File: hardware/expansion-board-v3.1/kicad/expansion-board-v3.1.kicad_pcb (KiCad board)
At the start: 6 copper layers, 100 x 62 mm, 156 parts, among them J1 PinHeader_2x20_P2.54mm_Vertic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, J2 U.FL_Hirose_U.FL-R-SMT-1_Vert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, J4 USB_C_Receptacle_HRO_TYPE-C-3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, J5 U.FL_Hirose_U.FL-R-SMT-1_Vert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, J6 U.FL_Hirose_U.FL-R-SMT-1_Vert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, J8 U.FL_Hirose_U.FL-R-SMT-1_Vert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, Q2 SOT-23, Q3 SOT-23, Q4 SOT-23, Q5 SOT-23, SW1 SolderJumper-2_P1.3mm_Open_Pa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, SW2 SolderJumper-2_P1.3mm_Open_Pa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, U1 SOT-23-5, U10 QFN-48-1EP_7x7mm_P0.5mm_EP5.1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, U11 DFN-8-1EP_2x2mm_P0.5mm_EP0.86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, U12 SOT-363_SC-70-6, U13 AD8319_LFCSP-8-EP, U14 MSOP-8_3x3mm_P0.65mm, U15 SOT-23-6, U16 SOT-363_SC-70-6, U17 SOT-363_SC-70-6, U2 SOT-23-5, U3 SOT-23-5, U4 BNO085_LGA-28, U5 BMP388_LGA-10, U6 LGA-16_3x3mm_P0.5mm, U7 ATGM336H_LCC-18, U8 QFN-56-1EP_7x7mm_P0.4mm_EP3.2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, U9 SOIC-8_5.3x5.3mm_P1.27mm, Y1 Crystal_SMD_3225-4Pin_3.2x2.5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, Y2 Crystal_SMD_3225-4Pin_3.2x2.5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, Y3 Crystal_SMD_3215-2Pin_3.2x1.5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

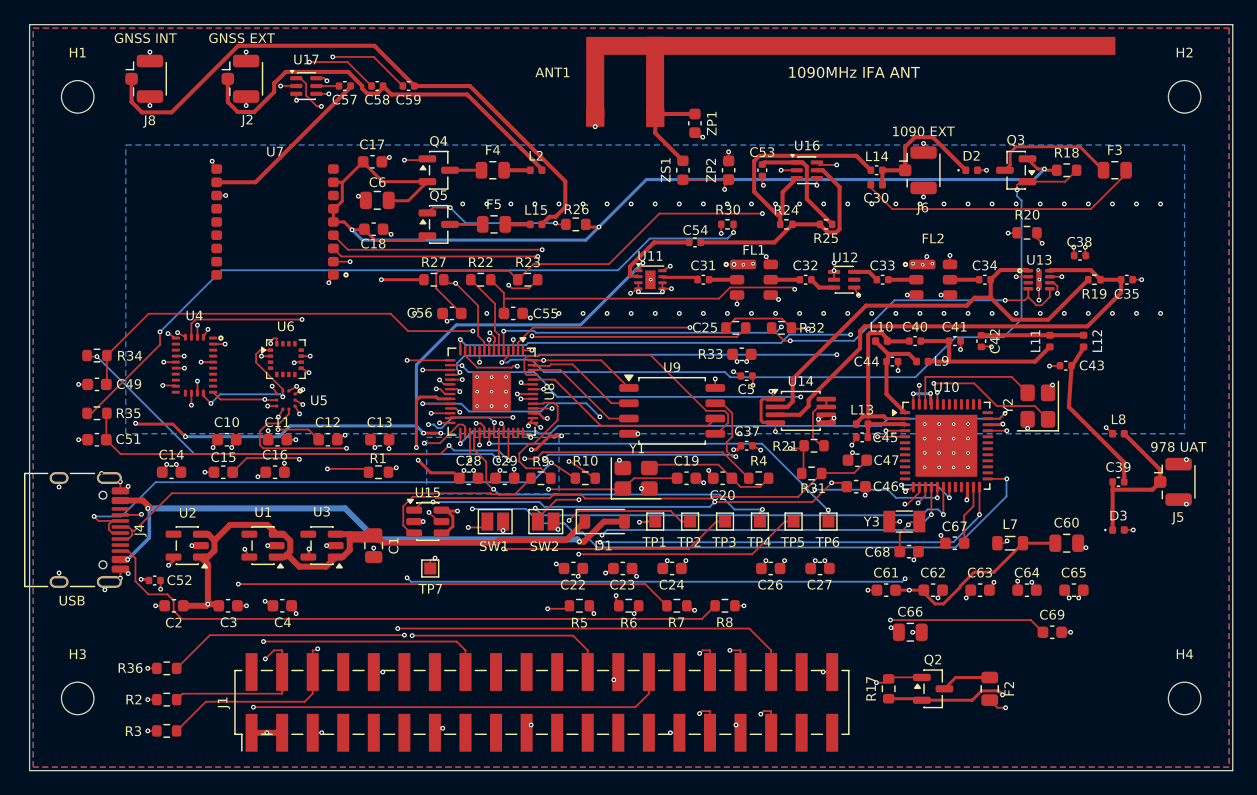
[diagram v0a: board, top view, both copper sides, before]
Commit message: feat(hw): 重排布局布线 + IC 型号标注 —— 全绿，Gerber 已出
评审挪了元件、重拉了线、删掉重排了自动生成的走线、加了 GND 缝合孔，
要求检查 + 在 IC 中心标型号 + 固化 + 出 Gerber。

    未连通 0 / 铜层 DRC 0 违例 / 丝印 overlap 1 / over_copper 1 / edge 2
    走线 1428 段 / 过孔 469 个   射频 165 段全 F.Cu、0 过孔
    rebuild 逐坐标 100% 复现（走线/过孔/板级文字/位号/元件坐标全部 0 不一致）

## 检查出 7 项并全部修掉

  · holes_co_located ×3 —— 加 GND 孔时在 (97.012,57.727) 同一点叠了 3 个（重复点击）
  · track_dangling SUBG_FEED —— 0.27mm 残线，另一端已是三线交汇点，删掉不影响连通
  · track_dangling SUBG_N5 —— 两段在 82.275~82.860 重叠成 **T 接**。电气上是通的
    （未连通=0 证明），但 KiCad 要求端点对端点，端点落在另一条线**中间**判 dangling。
    把起点提到 82.860 与之首尾相接
  · clearance ×2 —— 新加的两个 GND 缝合孔离 SUBG_MISO 只有 0.1255mm（要 0.15）。
    缝合孔哪儿都能打，沿法向挪 0.10mm

删除时踩了个老坑：`board.Remove()` 之后在**同一进程**里跑 ZONE_FILLER，
被删的线又回来了（route_fix.py:26 记过 SWIG 状态不可靠）。拆成三个独立进程：
改坐标 → 删除 → 重灌，才真正生效。

## IC 型号标注：17 条，但只有 1 条能真印

新增 gen_u_labels.py。判据迭代了三轮，每轮都是被 DRC 打回来的：

  ① 只查中心点是否落在焊盘上 → 报 29 条 silk_over_copper
     文字**有宽度**，BNO085 那串宽 4.5mm 横跨整颗芯片、压住左右两排引脚
  ② 改用文字包围盒，但只试横排 → 17 颗里只有 2 颗能印
     **横排压焊盘不代表竖排也压**：SOT-23-5 这类两侧排焊盘的封装，
     中间那条竖缝往往容得下竖排
  ③ 横竖都试之后仍报 17 条 over_copper，两个原因：
     · **CHAR_W 取 0.62 严重低估** —— KiCad 描边字体字宽≈字高、加字距约 1.1×h。
       系数错了，后面所有几何判断都白算
     · hits() 只查元件**自己**的焊盘 —— 实测 U14 的 'AD8313' 压到了隔壁 R21

用正确的字宽算下来：**只有 U7(ATGM336H) 一颗印得上**。这是物理现实——
IC 中心两侧就是引脚焊盘，型号串放进去必然压焊盘。其余 16 条进 F.Fab：
不参与印刷、不影响制造，但 KiCad 里看得见、assembly-top.pdf 里有。
最终丝印违例**没有增加**（还是原有的 1/1/2），证明 17 条全部落在合法位置。

三路 LDO 的标注用**功能标识**而非型号（3V3-D / 3V3-RF / 3V3-G）：
TPS7A2033 放进 SOT-23-5 只有 0.70mm 字高、低于可印下限，而且对着空板调试时
想知道的本来就是"这颗出什么电"，料号在 BOM 和装配图里有。

## Gerber

fab/expansion-board-v3.1-fab.zip（18 个文件）+ positions.csv
硬门槛通过：未连通 0、铜层违例 0。
下单四项确认见 tools/gerber.sh 输出（6 层叠层顺序 / POFV 树脂塞孔 /
最小孔径线宽 0.15 / 板厚 1.6mm 无铅）。
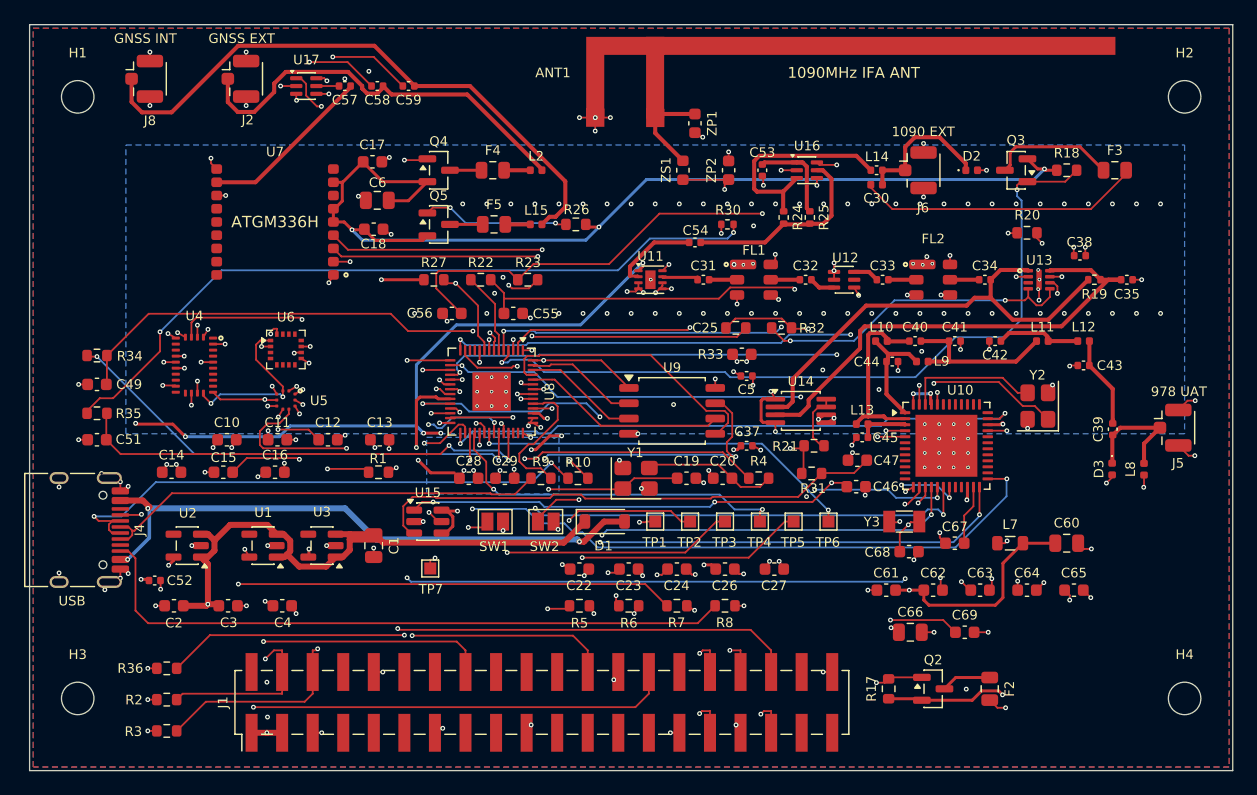
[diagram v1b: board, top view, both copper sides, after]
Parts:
- moved C69 7.28 mm to (127.7, 100.5)
- moved D3 5.09 mm to (140.0, 86.9), turned to -90 degrees
- moved J5 4.50 mm to (145.5, 83.5)
- moved C39 4.40 mm to (140.0, 83.6), turned to -90 degrees
- moved C26 3.80 mm to (107.8, 95.2)
- moved C27 3.80 mm to (111.9, 95.2)
- moved L8 3.64 mm to (142.6, 87.0), turned to 90 degrees
- moved C43 1.48 mm to (137.6, 78.3)
- moved R25 1.47 mm to (114.8, 66.0), turned to -90 degrees
- moved C42 1.15 mm to (130.2, 76.3), turned to 180 degrees
- moved U6 0.80 mm to (71.3, 77.0)
- moved L11 0.62 mm to (134.2, 76.3), turned to 0 degrees
- moved R24 0.62 mm to (112.7, 66.0), turned to -90 degrees
- moved R10 0.61 mm to (95.6, 87.7)
- moved C22 0.50 mm to (95.7, 95.2)
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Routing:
- net GND: track 100.1 -> 108.9 mm, vias 221 -> 237
- net SUBG_X32K2: track 32.7 -> 25.4 mm
- net SUBG_N5: track 13.6 -> 7.65 mm
- net ANT_978: track 13.5 -> 10.0 mm
- net SW1_J1: track 18.5 -> 16.4 mm
- net SUBG_VDDR: track 36.6 -> 38.6 mm
- net SW1_J3: track 9.59 -> 7.73 mm
- net SW1_J2: track 20.3 -> 18.4 mm
- net 3V3_DIG: track 37.9 -> 39.5 mm
- net SUBG_N4: track 8.50 -> 7.13 mm
- net SUBG_FEED: track 29.1 -> 27.7 mm
- net USB_CC2: track 53.8 -> 55.1 mm
- net SUBG_N3: track 14.8 -> 13.8 mm
- net QMC_C1: track 15.2 -> 16.0 mm
- net I2C_SCL: track 52.1 -> 52.9 mm
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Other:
- board text added: "3V3-D"
- board text added: "3V3-G"
- board text added: "3V3-RF"
- board text added: "AD8313"
- board text added: "AD8319"
- board text added: "ATGM336H"
- board text added: "BMP388"
- board text added: "BNO085"
- board text added: "CC1312R"
- board text added: "LNA1"
- board text added: "LNA2"
- board text added: "QMC5883"
- board text added: "RP2040"
- board text added: "SW1090"
- board text added: "SWGNSS"
- board text added: "TLV3501"
- board text added: "W25Q128"

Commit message: fix(hw): 板子版本号 V1 → V1.0，重出 Gerber
产品要求：「板子的版本号是 1.0，改过来，然后重新生成 Gerber」。

改了三处，缺一处版本号就会不一致：
    tools/gen_silk.py       BOARD_REV      离线排版工具
    tools/gen_brand_silk.py BOARD_REV      流程里补品牌丝印用
    tools/SILK.json         'V1   2026-08' → 'V1.0   2026-08'

**SILK.json 才是板子的真正来源**——rebuild 从它复现板级文字，
只改两个脚本的常量而不改它，跑一次 rebuild 版本号又变回 V1。

验证：rebuild 后板上 B.Silkscreen (100.0,80.0) 是 'V1.0   2026-08' ✅
    未连通 0 / 铜层 DRC 0 / 丝印 1+1+2（与改版本号前一致）

Gerber 已重出：fab/expansion-board-v3.1-fab.zip（645KB，18 个文件）
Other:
- board text added: "V1.0 2026-08"
- board text removed: "V1 2026-08"

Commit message: fix(hw): 板子版本号改为 V3.1（上一版写成 1.0 是错的）
板子从工程名到目录名都是 v3.1，丝印上写 V1.0 对不上。

改的还是那三处（缺一处，跑一次 rebuild 就退回去）：
    tools/gen_silk.py       BOARD_REV
    tools/gen_brand_silk.py BOARD_REV
    tools/SILK.json         ← 这个才是板子的来源，rebuild 从它复现板级文字

验证：板上 B.Silkscreen (100.0,80.0) = 'V3.1   2026-08'
    未连通 0 / 铜层 DRC 0 / 丝印 1+1+2（与改动前一致）
Gerber 已重出。
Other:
- board text added: "V3.1 2026-08"
- board text removed: "V1.0 2026-08"

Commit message: fix(hw): 最小孔径 0.15 → 0.20mm，省掉嘉立创 200 元工艺费
评审下单时发现：最小孔径选 0.15mm 要**额外加收 200 元**，5 片打样从 300 涨到 500+。

## 那 34 个 0.15mm 孔本来就不该是 0.15

全是 EP 散热孔（thermal_vias.py 用 0.3mm 盘 / 0.15mm 孔），当初的理由是
"盘小才排得密"。但孔心间距后来已经从 0.8mm 放宽到 1.2mm（业界推荐上限），
**1.2mm 间距下 0.4mm 盘和 0.3mm 盘都排得开**——"排得密"这个理由早就不成立了，
等于白付这笔钱。

改完全板过孔统一成 0.4mm 盘 / 0.2mm 孔（466 个），**最小孔径 0.20mm 属普通档**，
不光这次省 200，将来批量下单也一直省着。

    改 31 个：U10 ×16、U8 ×9、FL2 ×3、FL1 ×2、U11 ×1
    删  3 个：U13

## 为什么 U13 那 3 个是删不是改

U13(AD8319) 的 EP 只有 **0.45mm 宽**，而嘉立创要求 0.2mm 孔至少配 0.4mm 盘
（环宽 0.1mm），两边只剩 0.025mm，放不下。

代价可接受：AD8319 是检波器、功耗几十毫瓦，散热完全不需要；EP 顶层仍连在 F.Cu
的 GND 覆铜上，只是少了直下内层地平面的低阻抗路径，射频地回流绕远一点。
这次是原型 5 片，验证完再决定要不要为这 3 个孔付钱。

## 顺带同步 gerber.sh 的下单提示

那几行是供照着勾选项的，写着"最小孔径 0.15mm"和"必须勾 POFV 树脂塞孔"
就白改了。POFV 也不再需要——盘中孔已经从 0.3mm 盘放大到 0.4mm。

验证：未连通 0 / 铜层 DRC 0 / 丝印 1+1+2，全板最小钻孔 0.20mm。
Gerber 已重出。
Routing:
- net GND: vias 237 -> 234
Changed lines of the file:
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@@
 	(via
 		(at 110.13 69.86)
-		(size 0.3)
-		(drill 0.15)
+		(size 0.4)
+		(drill 0.2)
 		(layers "F.Cu" "B.Cu")
 		(net "GND")
@@
 	(via
 		(at 125.6 86.8)
-		(size 0.3)
-		(drill 0.15)
-		(layers "F.Cu" "B.Cu")
-		(net "GND")
-	)
-	(via
-		(at 133.83 71.985)
-		(size 0.3)
-		(drill 0.15)
+		(size 0.4)
+		(drill 0.2)
 		(layers "F.Cu" "B.Cu")
 		(net "GND")
@@
 	(via
 		(at 126.8 83.2)
-		(size 0.3)
-		(drill 0.15)
+		(size 0.4)
+		(drill 0.2)
 		(layers "F.Cu" "B.Cu")
 		(net "GND")
@@
 	(via
 		(at 89.6 79.3)
-		(size 0.3)
-		(drill 0.15)
+		(size 0.4)
+		(drill 0.2)
 		(layers "F.Cu" "B.Cu")
 		(net "GND")
@@
 	(via
 		(at 125.6 83.2)
-		(size 0.3)
-		(drill 0.15)
+		(size 0.4)
+		(drill 0.2)
 		(layers "F.Cu" "B.Cu")
 		(net "GND")
@@
 	(via
 		(at 89.6 80.5)
-		(size 0.3)
-		(drill 0.15)
+		(size 0.4)
+		(drill 0.2)
 		(layers "F.Cu" "B.Cu")
 		(net "GND")
@@
 	(via
 		(at 124.4 83.2)
-		(size 0.3)
-		(drill 0.15)
+		(size 0.4)
+		(drill 0.2)
 		(layers "F.Cu" "B.Cu")
 		(net "GND")
@@
 	(via
 		(at 87.2 81.7)
-		(size 0.3)
-		(drill 0.15)
+		(size 0.4)
+		(drill 0.2)
 		(layers "F.Cu" "B.Cu")
 		(net "GND")
@@
 	(via
 		(at 88.4 80.5)
-		(size 0.3)
-		(drill 0.15)
+		(size 0.4)
+		(drill 0.2)
 		(layers "F.Cu" "B.Cu")
 		(net "GND")
@@
 	(via
 		(at 128 84.4)
-		(size 0.3)
-		(drill 0.15)
+		(size 0.4)
+		(drill 0.2)
 		(layers "F.Cu" "B.Cu")
 		(net "GND")
@@
 	(via
 		(at 128 83.2)
-		(size 0.3)
-		(drill 0.15)
+		(size 0.4)
+		(drill 0.2)
 		(layers "F.Cu" "B.Cu")
 		(net "GND")
@@
 	(via
 		(at 125.03 69.86)
-		(size 0.3)
-		(drill 0.15)
+		(size 0.4)
+		(drill 0.2)
 		(layers "F.Cu" "B.Cu")
 		(net "GND")
@@
 	(via
 		(at 87.2 79.3)
-		(size 0.3)
-		(drill 0.15)
+		(size 0.4)
+		(drill 0.2)
 		(layers "F.Cu" "B.Cu")
 		(net "GND")
@@
 	(via
 		(at 125.6 84.4)
-		(size 0.3)
-		(drill 0.15)
+		(size 0.4)
+		(drill 0.2)
 		(layers "F.Cu" "B.Cu")
 		(net "GND")
@@
 	(via
 		(at 124.4 84.4)
-		(size 0.3)
-		(drill 0.15)
-		(layers "F.Cu" "B.Cu")
-		(net "GND")
-	)
-	(via
-		(at 133.83 70.385)
-		(size 0.3)
-		(drill 0.15)
+		(size 0.4)
+		(drill 0.2)
 		(layers "F.Cu" "B.Cu")
 		(net "GND")
@@
 	(via
 		(at 87.2 80.5)
-		(size 0.3)
-		(drill 0.15)
+		(size 0.4)
+		(drill 0.2)
 		(layers "F.Cu" "B.Cu")
 		(net "GND")
@@
 	(via
 		(at 89.6 81.7)
-		(size 0.3)
-		(drill 0.15)
+		(size 0.4)
+		(drill 0.2)
 		(layers "F.Cu" "B.Cu")
 		(net "GND")
@@
 	(via
 		(at 88.4 79.3)
-		(size 0.3)
-		(drill 0.15)
+		(size 0.4)
+		(drill 0.2)
 		(layers "F.Cu" "B.Cu")
 		(net "GND")
@@
 	(via
 		(at 124.4 86.8)
-		(size 0.3)
-		(drill 0.15)
+		(size 0.4)
+		(drill 0.2)
 		(layers "F.Cu" "B.Cu")
 		(net "GND")
@@
 	(via
 		(at 124.23 69.96)
-		(size 0.3)
-		(drill 0.15)
+		(size 0.4)
+		(drill 0.2)
 		(layers "F.Cu" "B.Cu")
 		(net "GND")
@@
 	(via
 		(at 124.4 85.6)
-		(size 0.3)
-		(drill 0.15)
+		(size 0.4)
+		(drill 0.2)
 		(layers "F.Cu" "B.Cu")
 		(net "GND")
@@
 	(via
 		(at 126.8 85.6)
-		(size 0.3)
-		(drill 0.15)
+		(size 0.4)
+		(drill 0.2)
 		(layers "F.Cu" "B.Cu")
 		(net "GND")
@@
 	(via
 		(at 101.63 71.185)
-		(size 0.3)
-		(drill 0.15)
+		(size 0.4)
+		(drill 0.2)
 		(layers "F.Cu" "B.Cu")
 		(net "GND")
@@
 	(via
 		(at 126.8 84.4)
-		(size 0.3)
-		(drill 0.15)
+		(size 0.4)
+		(drill 0.2)
 		(layers "F.Cu" "B.Cu")
 		(net "GND")
@@
 	(via
 		(at 123.43 69.86)
-		(size 0.3)
-		(drill 0.15)
+		(size 0.4)
+		(drill 0.2)
 		(layers "F.Cu" "B.Cu")
 		(net "GND")
@@
 	(via
 		(at 109.33 69.96)
-		(size 0.3)
-		(drill 0.15)
+		(size 0.4)
+		(drill 0.2)
 		(layers "F.Cu" "B.Cu")
 		(net "GND")
@@
 	(via
 		(at 128 86.8)
-		(size 0.3)
-		(drill 0.15)
+		(size 0.4)
+		(drill 0.2)
 		(layers "F.Cu" "B.Cu")
 		(net "GND")
@@
 	)
 	(via
-		(at 133.93 71.185)
-		(size 0.3)
-		(drill 0.15)
-		(layers "F.Cu" "B.Cu")
-		(net "GND")
-	)
-	(via
 		(at 112 74)
 		(size 0.4)
@@
 	(via
 		(at 126.8 86.8)
-		(size 0.3)
-		(drill 0.15)
+		(size 0.4)
+		(drill 0.2)
 		(layers "F.Cu" "B.Cu")
 		(net "GND")
@@
 	(via
 		(at 128 85.6)
-		(size 0.3)
-		(drill 0.15)
+		(size 0.4)
+		(drill 0.2)
 		(layers "F.Cu" "B.Cu")
 		(net "GND")
@@
 	(via
 		(at 125.6 85.6)
-		(size 0.3)
-		(drill 0.15)
+		(size 0.4)
+		(drill 0.2)
 		(layers "F.Cu" "B.Cu")
 		(net "GND")
@@
 	(via
 		(at 88.4 81.7)
-		(size 0.3)
-		(drill 0.15)
-		(layers "F.Cu" "B.Cu")
-		(net "GND")
+		(size 0.4)
+		(drill 0.2)
+		(layers "F.Cu" "B.Cu")
+		(net "GND")
